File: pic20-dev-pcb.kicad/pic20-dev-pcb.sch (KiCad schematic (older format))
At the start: 21 parts, among them J1 PGM-Conn, J2 App_Conn_1, J3 App_Conn_2, J4 Conn_SR, J5 Conn_01x03_Male, J6 Conn_BB1, J7 Conn_01x03_Male, SW1 SW_Push, U1 PIC16F1829-IP, U2 TLV1117-33

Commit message: pic20-dev-pcb: Rev 1.2: use DIP-20 footprint for PIC
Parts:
- C1: footprint Capacitor_SMD:C_1206_3216Metric -> Capacitor_SMD:C_0805_2012Metric
- D1, D2: footprint LED_SMD:LED_1206_3216Metric -> LED_SMD:LED_0805_2012Metric
- J2: footprint Connector_PinHeader_2.54mm:PinHeader_1x10_P2.54mm_Vertical -> Connector_PinHeader_2.54mm:PinHeader_1x09_P2.54mm_Vertical; symbol Connector:Conn_01x10_Male -> Connector:Conn_01x09_Male
- J3: footprint Connector_PinHeader_2.54mm:PinHeader_1x10_P2.54mm_Vertical -> Connector_PinHeader_2.54mm:PinHeader_1x11_P2.54mm_Vertical; symbol Connector:Conn_01x10_Male -> Connector:Conn_01x11_Male
- R1, R2: footprint Resistor_SMD:R_1206_3216Metric_Pad1.42x1.75mm_HandSolder -> Resistor_SMD:R_0805_2012Metric
- R3, R4: footprint Resistor_SMD:R_1206_3216Metric_Pad1.30x1.75mm_HandSolder -> Resistor_SMD:R_0805_2012Metric
- U1: footprint Socket:DIP_Socket-20_W4.3_W5.08_W7.62_W10.16_W10.9_3M_220-3342-00-0602J -> Package_DIP:DIP-20_W7.62mm
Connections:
- net +VDD: now also J3.1 (Pin_1); no longer J2.1 (Pin_1)
- net GND: now also J3.2 (Pin_2); no longer J3.1 (Pin_1)
- net RA0: now also J3.3 (Pin_3); no longer J3.2 (Pin_2)
- net RA1: now also J3.4 (Pin_4); no longer J3.3 (Pin_3)
- net RA2: now also J3.5 (Pin_5); no longer J3.4 (Pin_4)
- net RA3: now also J2.3 (Pin_3); no longer J2.4 (Pin_4)
- net RA4: now also J2.2 (Pin_2); no longer J2.3 (Pin_3)
- net RA5: now also J2.1 (Pin_1); no longer J2.2 (Pin_2)
- net RB4: now also J3.9 (Pin_9); no longer J3.8 (Pin_8)
- net RB5: now also J3.10 (Pin_10); no longer J3.9 (Pin_9)
- net RB6: now also J3.11 (Pin_11); no longer J3.10 (Pin_10)
- net RB7: now also J2.9 (Pin_9); no longer J2.10 (Pin_10)
- net RC0: now also J3.6 (Pin_6); no longer J3.5 (Pin_5)
- net RC1: now also J3.7 (Pin_7); no longer J3.6 (Pin_6)
- net RC2: now also J3.8 (Pin_8); no longer J3.7 (Pin_7)
- net RC3: now also J2.6 (Pin_6); no longer J2.7 (Pin_7)
- net RC4: now also J2.5 (Pin_5); no longer J2.6 (Pin_6)
- net RC5: now also J2.4 (Pin_4); no longer J2.5 (Pin_5)
- net RC6: now also J2.7 (Pin_7); no longer J2.8 (Pin_8)
- net RC7: now also J2.8 (Pin_8); no longer J2.9 (Pin_9)
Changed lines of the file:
@@
 Title "PIC20-Development Breadboard-PCB"
 Date "2021-04-20"
-Rev "1.1"
+Rev "1.2"
 Comp "Bernhard Bablok"
 Comment1 "https://github.com/bablokb/pcb-pic-devboard"
@@
 F 0 "C1" H 5565 3846 50  0000 L CNN
 F 1 "100nF" H 5565 3755 50  0000 L CNN
-F 2 "Capacitor_SMD:C_1206_3216Metric" H 5488 3650 50  0001 C CNN
+F 2 "Capacitor_SMD:C_0805_2012Metric" H 5488 3650 50  0001 C CNN
 F 3 "~" H 5450 3800 50  0001 C CNN
 	1    5450 3800
@@
 F 0 "R1" V 3700 4450 50  0000 C CNN
 F 1 "1K" V 3750 4600 50  0000 C CNN
-F 2 "Resistor_SMD:R_1206_3216Metric_Pad1.42x1.75mm_HandSolder" V 3680 4600 50  0001 C CNN
+F 2 "Resistor_SMD:R_0805_2012Metric" V 3680 4600 50  0001 C CNN
 F 3 "~" H 3750 4600 50  0001 C CNN
 	1    3750 4600
@@
 F 0 "R2" V 3800 4550 50  0000 C CNN
 F 1 "1K" V 3750 4700 50  0000 C CNN
-F 2 "Resistor_SMD:R_1206_3216Metric_Pad1.42x1.75mm_HandSolder" V 3680 4700 50  0001 C CNN
+F 2 "Resistor_SMD:R_0805_2012Metric" V 3680 4700 50  0001 C CNN
 F 3 "~" H 3750 4700 50  0001 C CNN
 	1    3750 4700
@@
 F 0 "R3" V 1950 6750 50  0000 C CNN
 F 1 "1kΩ" V 1850 6750 50  0000 C CNN
-F 2 "Resistor_SMD:R_1206_3216Metric_Pad1.30x1.75mm_HandSolder" V 1780 6750 50  0001 C CNN
+F 2 "Resistor_SMD:R_0805_2012Metric" V 1780 6750 50  0001 C CNN
 F 3 "~" H 1850 6750 50  0001 C CNN
 	1    1850 6750
@@
 F 0 "D1" H 2150 6850 50  0000 C CNN
 F 1 "LED" H 2150 6650 50  0000 C CNN
-F 2 "LED_SMD:LED_1206_3216Metric" H 2150 6750 50  0001 C CNN
+F 2 "LED_SMD:LED_0805_2012Metric" H 2150 6750 50  0001 C CNN
 F 3 "~" H 2150 6750 50  0001 C CNN
 	1    2150 6750
@@
 F 0 "R4" V 1950 6400 50  0000 C CNN
 F 1 "1kΩ" V 1850 6400 50  0000 C CNN
-F 2 "Resistor_SMD:R_1206_3216Metric_Pad1.30x1.75mm_HandSolder" V 1780 6400 50  0001 C CNN
+F 2 "Resistor_SMD:R_0805_2012Metric" V 1780 6400 50  0001 C CNN
 F 3 "~" H 1850 6400 50  0001 C CNN
 	1    1850 6400
@@
 F 0 "D2" H 2150 6500 50  0000 C CNN
 F 1 "LED" H 2150 6300 50  0000 C CNN
-F 2 "LED_SMD:LED_1206_3216Metric" H 2150 6400 50  0001 C CNN
+F 2 "LED_SMD:LED_0805_2012Metric" H 2150 6400 50  0001 C CNN
 F 3 "~" H 2150 6400 50  0001 C CNN
 	1    2150 6400
@@
 F 0 "U1" H 5900 6100 50  0000 C CNN
 F 1 "PIC16F1829-IP" H 5950 5950 50  0000 C CNN
-F 2 "Socket:DIP_Socket-20_W4.3_W5.08_W7.62_W10.16_W10.9_3M_220-3342-00-0602J" H 5450 4550 50  0001 C CNN
+F 2 "Package_DIP:DIP-20_W7.62mm" H 5450 4550 50  0001 C CNN
 F 3 "http://ww1.microchip.com/downloads/en/DeviceDoc/41440C.pdf" H 5450 4550 50  0001 C CNN
 	1    5450 5100
@@
 	4550 4100 5450 4100
 $Comp
-L Connector:Conn_01x10_Male J2
+L Connector:Conn_01x09_Male J2
 U 1 1 607EC51A
-P 7800 5000
-F 0 "J2" H 7900 5750 50  0000 C CNN
-F 1 "App_Conn_1" H 7950 5600 50  0000 C CNN
-F 2 "Connector_PinHeader_2.54mm:PinHeader_1x10_P2.54mm_Vertical" H 7800 5000 50  0001 C CNN
-F 3 "~" H 7800 5000 50  0001 C CNN
-	1    7800 5000
-	1    0    0    -1
-$EndComp
-Text Label 8000 4900 0    50   ~ 0
+P 8000 4900
+F 0 "J2" H 8200 5600 50  0000 C CNN
+F 1 "App_Conn_1" H 8200 5500 50  0000 C CNN
+F 2 "Connector_PinHeader_2.54mm:PinHeader_1x09_P2.54mm_Vertical" H 8000 4900 50  0001 C CNN
+F 3 "~" H 8000 4900 50  0001 C CNN
+	1    8000 4900
+	1    0    0    -1
+$EndComp
+Text Label 8200 4700 0    50   ~ 0
 RA3
-Text Label 8000 4800 0    50   ~ 0
+Text Label 8200 4600 0    50   ~ 0
 RA4
-Text Label 8000 4700 0    50   ~ 0
+Text Label 8200 4500 0    50   ~ 0
 RA5
-Text Label 8000 5200 0    50   ~ 0
+Text Label 8200 5000 0    50   ~ 0
 RC3
-Text Label 8000 5100 0    50   ~ 0
+Text Label 8200 4900 0    50   ~ 0
 RC4
-Text Label 8000 5000 0    50   ~ 0
+Text Label 8200 4800 0    50   ~ 0
 RC5
-Text Label 8000 5300 0    50   ~ 0
+Text Label 8200 5100 0    50   ~ 0
 RC6
-Text Label 8000 5500 0    50   ~ 0
+Text Label 8200 5300 0    50   ~ 0
 RB7
-Text Label 8000 5400 0    50   ~ 0
+Text Label 8200 5200 0    50   ~ 0
 RC7
 $Comp
-L Connector:Conn_01x10_Male J3
+L Connector:Conn_01x11_Male J3
 U 1 1 607F7A8D
 P 8850 5000
-F 0 "J3" H 8950 5750 50  0000 C CNN
-F 1 "App_Conn_2" H 9000 5600 50  0000 C CNN
-F 2 "Connector_PinHeader_2.54mm:PinHeader_1x10_P2.54mm_Vertical" H 8850 5000 50  0001 C CNN
+F 0 "J3" H 8950 5800 50  0000 C CNN
+F 1 "App_Conn_2" H 9000 5700 50  0000 C CNN
+F 2 "Connector_PinHeader_2.54mm:PinHeader_1x11_P2.54mm_Vertical" H 8850 5000 50  0001 C CNN
 F 3 "~" H 8850 5000 50  0001 C CNN
 	1    8850 5000
@@
 	0    -1   -1   0
 $EndComp
-Text Label 8000 4600 0    50   ~ 0
+Wire Wire Line
+	9050 4600 9300 4600
+Text Label 9050 4500 0    50   ~ 0
 +VDD
-Wire Wire Line
-	9050 4600 9300 4600
 $EndSCHEMATC

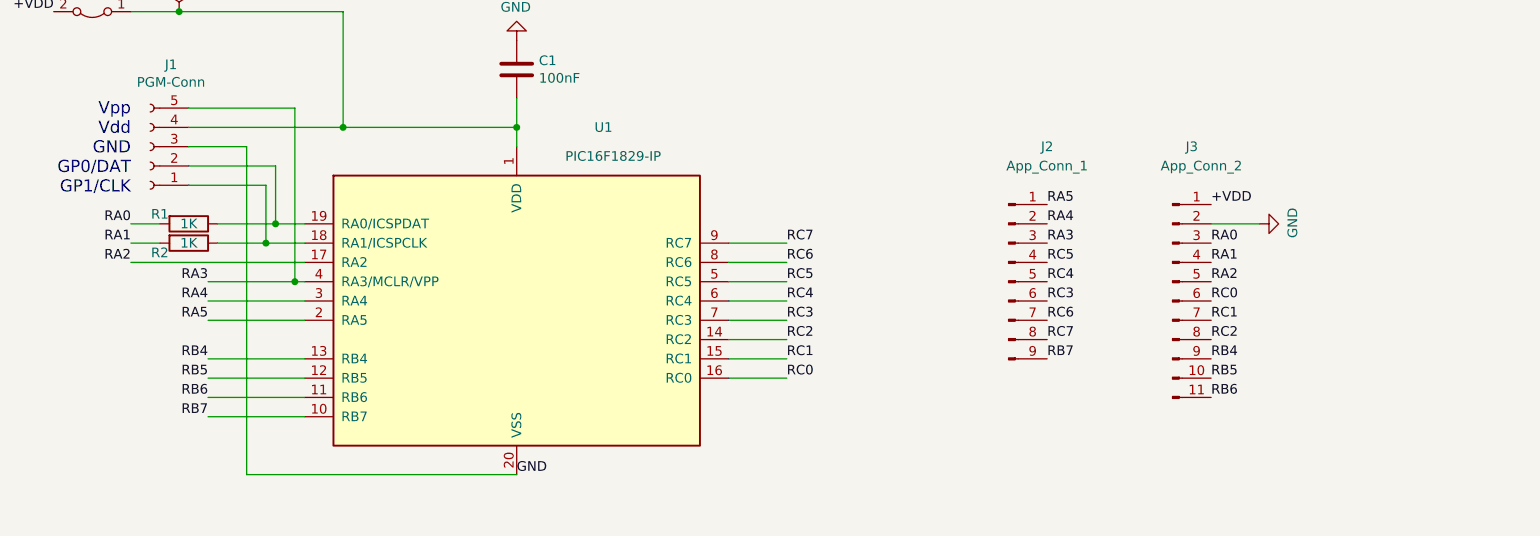
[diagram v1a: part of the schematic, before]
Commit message: pic20-dev-pcb: Rev 1.3: add SPI-connector, use socket for PIC
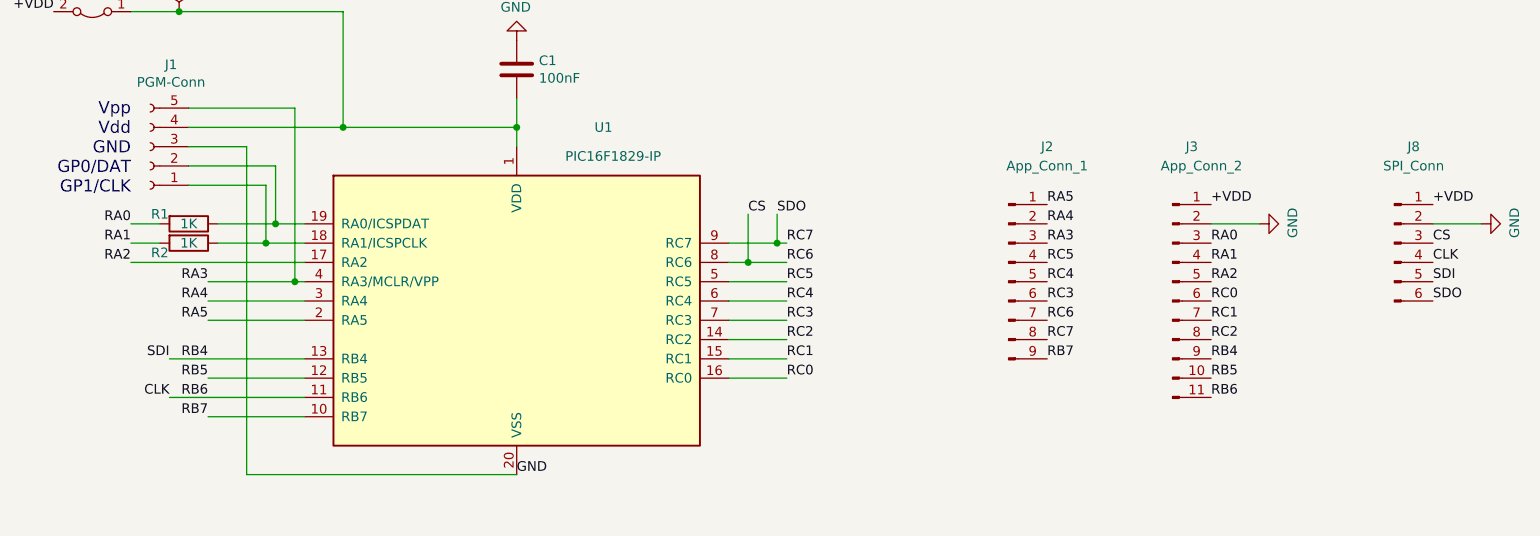
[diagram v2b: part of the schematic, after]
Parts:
- added J8: SPI_Conn, Connector_PinHeader_2.54mm:PinHeader_1x06_P2.54mm_Vertical, symbol Connector:Conn_01x06_Male
- U1: footprint Package_DIP:DIP-20_W7.62mm -> Package_DIP:DIP-20_W7.62mm_Socket
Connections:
- net +VDD: now also J8.1 (Pin_1)
- net GND: now also J8.2 (Pin_2)
- net RB4: now also J8.5 (Pin_5)
- net RC7: now also J8.6 (Pin_6)
- net RB6 renamed CLK
- net CLK: now also J8.4 (Pin_4)
- net RC6 renamed CS
- net CS: now also J8.3 (Pin_3)
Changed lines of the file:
@@
 Sheet 1 1
 Title "PIC20-Development Breadboard-PCB"
-Date "2021-04-20"
-Rev "1.2"
+Date "2021-04-21"
+Rev "1.3"
 Comp "Bernhard Bablok"
 Comment1 "https://github.com/bablokb/pcb-pic-devboard"
@@
 F 0 "U1" H 5900 6100 50  0000 C CNN
 F 1 "PIC16F1829-IP" H 5950 5950 50  0000 C CNN
-F 2 "Package_DIP:DIP-20_W7.62mm" H 5450 4550 50  0001 C CNN
+F 2 "Package_DIP:DIP-20_W7.62mm_Socket" H 5450 4550 50  0001 C CNN
 F 3 "http://ww1.microchip.com/downloads/en/DeviceDoc/41440C.pdf" H 5450 4550 50  0001 C CNN
 	1    5450 5100
@@
 	3850 5100 4350 5100
 Wire Wire Line
-	3850 5300 4350 5300
-Wire Wire Line
 	3850 5400 4350 5400
-Wire Wire Line
-	3850 5500 4350 5500
 Wire Wire Line
 	3850 5600 4350 5600
@@
 RC0
 Wire Wire Line
-	6550 4700 6850 4700
-Wire Wire Line
-	6550 4800 6850 4800
+	6550 4700 6800 4700
+Wire Wire Line
+	6550 4800 6650 4800
 Wire Wire Line
 	6550 4900 6850 4900
@@
 Text Label 9050 4500 0    50   ~ 0
 +VDD
+$Comp
+L Connector:Conn_01x06_Male J8
+U 1 1 60824EA3
+P 10000 4700
+F 0 "J8" H 10100 5200 50  0000 C CNN
+F 1 "SPI_Conn" H 10100 5100 50  0000 C CNN
+F 2 "Connector_PinHeader_2.54mm:PinHeader_1x06_P2.54mm_Vertical" H 10000 4700 50  0001 C CNN
+F 3 "~" H 10000 4700 50  0001 C CNN
+	1    10000 4700
+	1    0    0    -1
+$EndComp
+Text Label 10200 4500 0    50   ~ 0
++VDD
+$Comp
+L power:GND #PWR03
+U 1 1 60828E41
+P 10450 4600
+F 0 "#PWR03" H 10450 4350 50  0001 C CNN
+F 1 "GND" H 10455 4427 50  0000 C CNN
+F 2 "" H 10450 4600 50  0001 C CNN
+F 3 "" H 10450 4600 50  0001 C CNN
+	1    10450 4600
+	0    -1   -1   0
+$EndComp
+Wire Wire Line
+	10200 4600 10450 4600
+Text Label 10200 4700 0    50   ~ 0
+CS
+Text Label 10200 4800 0    50   ~ 0
+CLK
+Text Label 10200 4900 0    50   ~ 0
+SDI
+Text Label 10200 5000 0    50   ~ 0
+SDO
+Text Label 6800 4550 0    50   ~ 0
+SDO
+Wire Wire Line
+	6800 4550 6800 4700
+Connection ~ 6800 4700
+Wire Wire Line
+	6800 4700 6850 4700
+Text Label 3650 5300 2    50   ~ 0
+SDI
+Wire Wire Line
+	3650 5300 4350 5300
+Text Label 3650 5500 2    50   ~ 0
+CLK
+Wire Wire Line
+	3650 5500 4350 5500
+Text Label 6650 4550 0    50   ~ 0
+CS
+Wire Wire Line
+	6650 4550 6650 4800
+Connection ~ 6650 4800
+Wire Wire Line
+	6650 4800 6850 4800
 $EndSCHEMATC

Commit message: updated footprint for micro-usb
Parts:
- USB1: footprint Connector_USB:USB_Micro-B_GCT_USB3076-30-A -> user:USB_Micro-B_JLCPCB_40942
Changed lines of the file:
@@
 F 0 "USB1" H 5750 1350 50  0000 L CNN
 F 1 "Micro-USB_Breakout" H 5500 1500 50  0000 L CNN
-F 2 "Connector_USB:USB_Micro-B_GCT_USB3076-30-A" H 5550 1900 50  0001 C CNN
+F 2 "user:USB_Micro-B_JLCPCB_40942" H 5550 1900 50  0001 C CNN
 F 3 "~" H 5550 1900 50  0001 C CNN
 	1    5550 1900

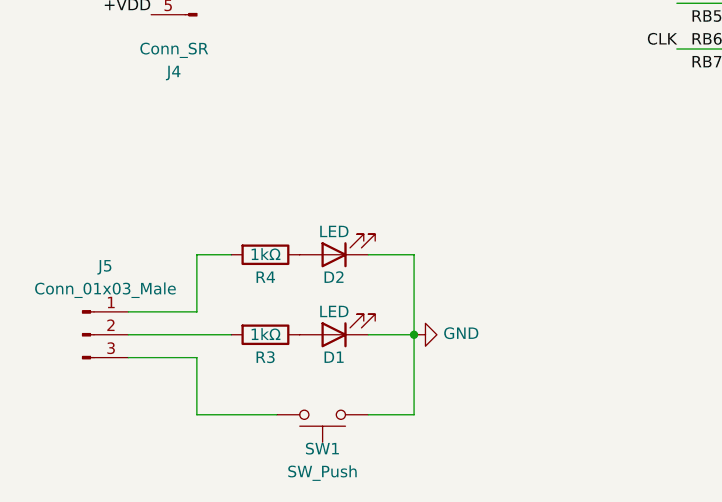
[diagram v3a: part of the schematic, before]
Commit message: pic20-dev-pcb: Rev 1.4: optimizations, prep for production
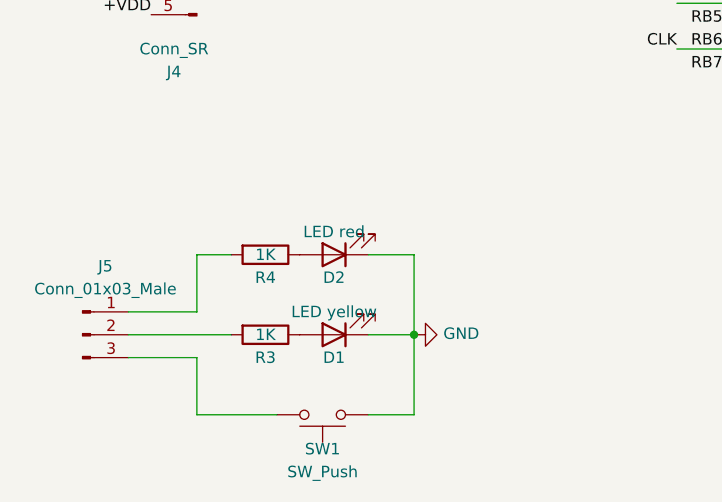
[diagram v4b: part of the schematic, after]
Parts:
- C1: LCSC (none) -> C49678
- C2, C3: LCSC (none) -> C7171
- D1: value LED -> LED yellow; LCSC (none) -> C2296
- D2: value LED -> LED red; LCSC (none) -> C84256
- R1, R2: LCSC (none) -> C17513
- R3, R4: value 1kΩ -> 1K; LCSC (none) -> C17513
- U2: LCSC (none) -> C6186
- USB1: LCSC (none) -> C40942
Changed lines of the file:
@@
 Sheet 1 1
 Title "PIC20-Development Breadboard-PCB"
-Date "2021-04-21"
-Rev "1.3"
+Date "2021-04-27"
+Rev "1.4"
 Comp "Bernhard Bablok"
 Comment1 "https://github.com/bablokb/pcb-pic-devboard"
@@
 F 2 "Capacitor_SMD:C_0805_2012Metric" H 5488 3650 50  0001 C CNN
 F 3 "~" H 5450 3800 50  0001 C CNN
+F 4 "C49678" H 5450 3800 50  0001 C CNN "LCSC"
 	1    5450 3800
 	1    0    0    -1
@@
 F 2 "Resistor_SMD:R_0805_2012Metric" V 3680 4600 50  0001 C CNN
 F 3 "~" H 3750 4600 50  0001 C CNN
+F 4 "C17513" V 3750 4600 50  0001 C CNN "LCSC"
 	1    3750 4600
 	0    1    1    0
@@
 F 2 "Resistor_SMD:R_0805_2012Metric" V 3680 4700 50  0001 C CNN
 F 3 "~" H 3750 4700 50  0001 C CNN
+F 4 "C17513" V 3750 4700 50  0001 C CNN "LCSC"
 	1    3750 4700
 	0    1    1    0
@@
 F 2 "user:USB_Micro-B_JLCPCB_40942" H 5550 1900 50  0001 C CNN
 F 3 "~" H 5550 1900 50  0001 C CNN
+F 4 "C40942" H 5550 1900 50  0001 C CNN "LCSC"
 	1    5550 1900
 	-1   0    0    1
@@
 P 1850 6750
 F 0 "R3" V 1950 6750 50  0000 C CNN
-F 1 "1kΩ" V 1850 6750 50  0000 C CNN
+F 1 "1K" V 1850 6750 50  0000 C CNN
 F 2 "Resistor_SMD:R_0805_2012Metric" V 1780 6750 50  0001 C CNN
 F 3 "~" H 1850 6750 50  0001 C CNN
+F 4 "C17513" V 1850 6750 50  0001 C CNN "LCSC"
 	1    1850 6750
 	0    1    1    0
@@
 P 2150 6750
 F 0 "D1" H 2150 6850 50  0000 C CNN
-F 1 "LED" H 2150 6650 50  0000 C CNN
+F 1 "LED yellow" H 2150 6650 50  0000 C CNN
 F 2 "LED_SMD:LED_0805_2012Metric" H 2150 6750 50  0001 C CNN
 F 3 "~" H 2150 6750 50  0001 C CNN
+F 4 "C2296" H 2150 6750 50  0001 C CNN "LCSC"
 	1    2150 6750
 	-1   0    0    1
@@
 P 1850 6400
 F 0 "R4" V 1950 6400 50  0000 C CNN
-F 1 "1kΩ" V 1850 6400 50  0000 C CNN
+F 1 "1K" V 1850 6400 50  0000 C CNN
 F 2 "Resistor_SMD:R_0805_2012Metric" V 1780 6400 50  0001 C CNN
 F 3 "~" H 1850 6400 50  0001 C CNN
+F 4 "C17513" V 1850 6400 50  0001 C CNN "LCSC"
 	1    1850 6400
 	0    1    1    0
@@
 P 2150 6400
 F 0 "D2" H 2150 6500 50  0000 C CNN
-F 1 "LED" H 2150 6300 50  0000 C CNN
+F 1 "LED red" H 2150 6300 50  0000 C CNN
 F 2 "LED_SMD:LED_0805_2012Metric" H 2150 6400 50  0001 C CNN
 F 3 "~" H 2150 6400 50  0001 C CNN
+F 4 "C84256" H 2150 6400 50  0001 C CNN "LCSC"
 	1    2150 6400
 	-1   0    0    1
@@
 F 2 "Capacitor_Tantalum_SMD:CP_EIA-3216-18_Kemet-A" H 7038 1200 50  0001 C CNN
 F 3 "~" H 7000 1350 50  0001 C CNN
+F 4 "C7171" V 7000 1350 50  0001 C CNN "LCSC"
 	1    7000 1350
 	0    1    1    0
@@
 F 2 "Capacitor_Tantalum_SMD:CP_EIA-3216-18_Kemet-A" H 6738 1200 50  0001 C CNN
 F 3 "~" H 6700 1350 50  0001 C CNN
+F 4 "C7171" V 6700 1350 50  0001 C CNN "LCSC"
 	1    6700 1350
 	0    -1   -1   0
@@
 F 2 "Package_TO_SOT_SMD:SOT-223" H 6850 1700 50  0001 C CNN
 F 3 "http://www.ti.com/lit/ds/symlink/tlv1117.pdf" H 6850 1700 50  0001 C CNN
+F 4 "C6186" H 6850 1700 50  0001 C CNN "LCSC"
 	1    6850 1700
 	1    0    0    1

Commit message: Rev 1.5: bugfix Micro-USB connector
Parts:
- USB1: value Micro-USB_Breakout -> Micro-USB; symbol User:Micro-USB_Breakout -> Connector:USB_B_Micro
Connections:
- net GND: now also USB1.5 (GND), USB1.6 (Shield); no longer USB1.1 (Pin_1)
- net at C2.1, J7.1 (Pin_1), U2.3 (VI): now also USB1.1 (VBUS); no longer USB1.5 (Pin_5)
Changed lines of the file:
@@
 Sheet 1 1
 Title "PIC20-Development Breadboard-PCB"
-Date "2021-04-27"
-Rev "1.4"
+Date "2021-05-20"
+Rev "1.5"
 Comp "Bernhard Bablok"
 Comment1 "https://github.com/bablokb/pcb-pic-devboard"
@@
 L power:GND #PWR0102
 U 1 1 5F0642E9
-P 5850 2400
-F 0 "#PWR0102" H 5850 2150 50  0001 C CNN
-F 1 "GND" H 5950 2150 50  0000 R CNN
-F 2 "" H 5850 2400 50  0001 C CNN
-F 3 "" H 5850 2400 50  0001 C CNN
-	1    5850 2400
-	1    0    0    -1
+P 4750 1700
+F 0 "#PWR0102" H 4750 1450 50  0001 C CNN
+F 1 "GND" H 4850 1450 50  0000 R CNN
+F 2 "" H 4750 1700 50  0001 C CNN
+F 3 "" H 4750 1700 50  0001 C CNN
+	1    4750 1700
+	-1   0    0    1
 $EndComp
 Text Notes 3450 4450 2    63   ~ 0
@@
 $EndComp
 $Comp
-L User:Micro-USB_Breakout USB1
+L Connector:USB_B_Micro USB1
 U 1 1 5F660F6B
-P 5550 1900
-F 0 "USB1" H 5750 1350 50  0000 L CNN
-F 1 "Micro-USB_Breakout" H 5500 1500 50  0000 L CNN
-F 2 "user:USB_Micro-B_JLCPCB_40942" H 5550 1900 50  0001 C CNN
-F 3 "~" H 5550 1900 50  0001 C CNN
-F 4 "C40942" H 5550 1900 50  0001 C CNN "LCSC"
-	1    5550 1900
-	-1   0    0    1
-$EndComp
-NoConn ~ 5750 2000
-NoConn ~ 5750 1900
-NoConn ~ 5750 1800
-Wire Wire Line
-	5750 1700 5900 1700
-$Comp
-L power:PWR_FLAG #FLG0102
-U 1 1 5F6670F7
-P 5500 2400
-F 0 "#FLG0102" H 5500 2475 50  0001 C CNN
-F 1 "PWR_FLAG" H 5500 2650 50  0000 C CNN
-F 2 "" H 5500 2400 50  0001 C CNN
-F 3 "~" H 5500 2400 50  0001 C CNN
-	1    5500 2400
-	-1   0    0    1
-$EndComp
-$Comp
-L power:PWR_FLAG #FLG0103
-U 1 1 5F6676D5
-P 5900 1700
-F 0 "#FLG0103" H 5900 1775 50  0001 C CNN
-F 1 "PWR_FLAG" H 5900 1873 50  0000 C CNN
-F 2 "" H 5900 1700 50  0001 C CNN
-F 3 "~" H 5900 1700 50  0001 C CNN
-	1    5900 1700
-	1    0    0    -1
+P 5550 1150
+F 0 "USB1" V 5100 1000 50  0000 L CNN
+F 1 "Micro-USB" V 5250 950 50  0000 L CNN
+F 2 "user:USB_Micro-B_JLCPCB_40942" H 5550 1150 50  0001 C CNN
+F 3 "~" H 5550 1150 50  0001 C CNN
+F 4 "C40942" H 5550 1150 50  0001 C CNN "LCSC"
+	1    5550 1150
+	0    1    1    0
 $EndComp
 $Comp
@@
 	1    0    0    1
 $EndComp
-Wire Wire Line
-	5900 1700 6300 1700
-Connection ~ 5900 1700
 Connection ~ 6550 1700
-Wire Wire Line
-	5750 2100 5850 2100
 Wire Wire Line
 	6300 1700 6300 2550
@@
 	6700 3000 6200 3000
 Wire Wire Line
-	5850 2400 5500 2400
-Wire Wire Line
-	5850 2100 5850 2400
-Connection ~ 5850 2400
-Wire Wire Line
-	5500 2400 5150 2400
-Wire Wire Line
-	5150 2400 5150 1700
-Wire Wire Line
-	5150 1700 4050 1700
-Connection ~ 5500 2400
+	5150 1700 4750 1700
 Text Label 6200 2900 2    50   ~ 0
 +VDD
@@
 Wire Wire Line
 	6650 4800 6850 4800
+Wire Wire Line
+	5750 1700 5750 1450
+NoConn ~ 5550 1450
+NoConn ~ 5450 1450
+NoConn ~ 5350 1450
+Wire Wire Line
+	5150 1150 5150 1700
+Connection ~ 4750 1700
+Wire Wire Line
+	5150 1150 5150 1050
+Connection ~ 5150 1150
+Wire Wire Line
+	5750 1700 6300 1700
+Wire Wire Line
+	4050 1700 4750 1700
 $EndSCHEMATC
